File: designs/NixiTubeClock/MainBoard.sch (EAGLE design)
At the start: 17 parts, among them IC1 LD117ADT-TR, J1 S2B-PH-SM4, J2 S2B-PH-SM4, J3 S2B-PH-SM4, J4 S2B-PH-SM4, J7 S2B-PH-SM4, J8 S2B-PH-SM4

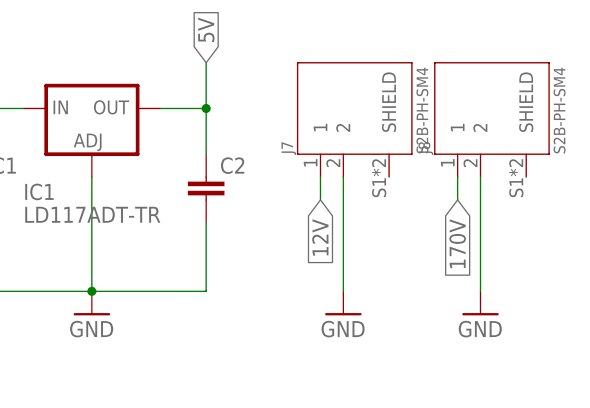
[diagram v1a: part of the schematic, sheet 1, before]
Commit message: added parts for nixi clock final check during the week
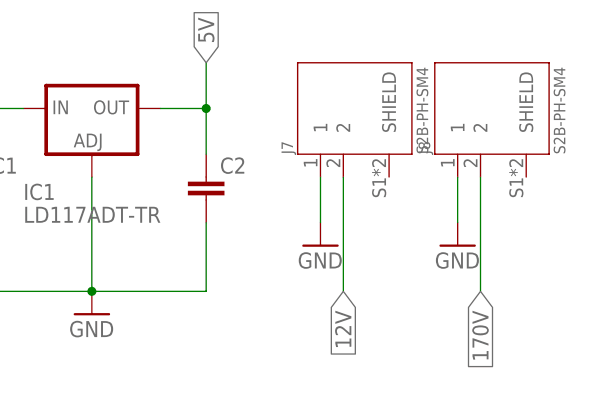
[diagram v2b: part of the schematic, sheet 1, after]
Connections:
- net 12V: now also J7.2; no longer J7.1
- net 170V: now also J8.2; no longer J8.1
- net GND: now also J7.1, J8.1; no longer J7.2, J8.2
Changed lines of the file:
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@@
 <?xml version="1.0" encoding="utf-8"?>
 <!DOCTYPE eagle SYSTEM "eagle.dtd">
-<eagle version="9.5.2">
+<eagle version="9.5.1">
 <drawing>
 <settings>
@@
 <part name="GND5" library="supply1" library_urn="urn:adsk.eagle:library:371" deviceset="GND" device=""/>
 <part name="GND6" library="supply1" library_urn="urn:adsk.eagle:library:371" deviceset="GND" device=""/>
-<part name="GND7" library="supply1" library_urn="urn:adsk.eagle:library:371" deviceset="GND" device=""/>
-<part name="GND8" library="supply1" library_urn="urn:adsk.eagle:library:371" deviceset="GND" device=""/>
 <part name="IC1" library="nixie_tube" deviceset="LD117A?*" device="DT" package3d_urn="urn:adsk.eagle:package:30369/1" technology="-TR"/>
 <part name="C1" library="CommonParts" deviceset="C-EU_1206" device="C1206" package3d_urn="urn:adsk.eagle:package:23618/2"/>
 <part name="C2" library="CommonParts" deviceset="C-EU_1206" device="C1206" package3d_urn="urn:adsk.eagle:package:23618/2"/>
 <part name="GND9" library="supply1" library_urn="urn:adsk.eagle:library:371" deviceset="GND" device=""/>
+<part name="GND8" library="supply1" library_urn="urn:adsk.eagle:library:371" deviceset="GND" device=""/>
+<part name="GND7" library="supply1" library_urn="urn:adsk.eagle:library:371" deviceset="GND" device=""/>
 </parts>
 <sheets>
@@
 <attribute name="VALUE" x="210.82" y="91.44" size="1.778" layer="96"/>
 </instance>
-<instance part="GND7" gate="1" x="193.04" y="48.26" smashed="yes">
-<attribute name="VALUE" x="190.5" y="45.72" size="1.778" layer="96"/>
-</instance>
-<instance part="GND8" gate="1" x="208.28" y="48.26" smashed="yes">
-<attribute name="VALUE" x="205.74" y="45.72" size="1.778" layer="96"/>
-</instance>
 <instance part="IC1" gate="G$1" x="165.1" y="71.12" smashed="yes">
 <attribute name="NAME" x="157.48" y="60.96" size="1.778" layer="95"/>
@@
 <instance part="GND9" gate="1" x="165.1" y="48.26" smashed="yes">
 <attribute name="VALUE" x="162.56" y="45.72" size="1.778" layer="96"/>
+</instance>
+<instance part="GND8" gate="1" x="190.5" y="55.88" smashed="yes">
+<attribute name="VALUE" x="187.96" y="53.34" size="1.778" layer="96"/>
+</instance>
+<instance part="GND7" gate="1" x="205.74" y="55.88" smashed="yes">
+<attribute name="VALUE" x="203.2" y="53.34" size="1.778" layer="96"/>
 </instance>
 </instances>
@@
 <wire x1="213.36" y1="109.22" x2="213.36" y2="96.52" width="0.1524" layer="91"/>
 <pinref part="GND6" gate="1" pin="GND"/>
-</segment>
-<segment>
-<pinref part="J7" gate="G$1" pin="2"/>
-<pinref part="GND7" gate="1" pin="GND"/>
-<wire x1="193.04" y1="50.8" x2="193.04" y2="63.5" width="0.1524" layer="91"/>
-</segment>
-<segment>
-<pinref part="J8" gate="G$1" pin="2"/>
-<pinref part="GND8" gate="1" pin="GND"/>
-<wire x1="208.28" y1="63.5" x2="208.28" y2="50.8" width="0.1524" layer="91"/>
 </segment>
 <segment>
@@
 <pinref part="SV4" gate="1" pin="5"/>
 </segment>
+<segment>
+<pinref part="GND8" gate="1" pin="GND"/>
+<pinref part="J7" gate="G$1" pin="1"/>
+<wire x1="190.5" y1="58.42" x2="190.5" y2="63.5" width="0.1524" layer="91"/>
+</segment>
+<segment>
+<pinref part="J8" gate="G$1" pin="1"/>
+<pinref part="GND7" gate="1" pin="GND"/>
+<wire x1="205.74" y1="58.42" x2="205.74" y2="63.5" width="0.1524" layer="91"/>
+</segment>
 </net>
 <net name="3.3V" class="0">
@@
 <net name="12V" class="0">
 <segment>
-<pinref part="J7" gate="G$1" pin="1"/>
-<wire x1="190.5" y1="63.5" x2="190.5" y2="60.96" width="0.1524" layer="91"/>
-<label x="190.5" y="60.96" size="1.778" layer="95" rot="R270" xref="yes"/>
-</segment>
-<segment>
 <pinref part="C1" gate="G$1" pin="1"/>
 <wire x1="152.4" y1="66.04" x2="152.4" y2="71.12" width="0.1524" layer="91"/>
@@
 <label x="152.4" y="76.2" size="1.778" layer="95" rot="R90" xref="yes"/>
 </segment>
+<segment>
+<pinref part="J7" gate="G$1" pin="2"/>
+<wire x1="193.04" y1="50.8" x2="193.04" y2="63.5" width="0.1524" layer="91"/>
+<label x="193.04" y="50.8" size="1.778" layer="95" rot="R270" xref="yes"/>
+</segment>
 </net>
 <net name="170V" class="0">
-<segment>
-<pinref part="J8" gate="G$1" pin="1"/>
-<wire x1="205.74" y1="63.5" x2="205.74" y2="60.96" width="0.1524" layer="91"/>
-<label x="205.74" y="60.96" size="1.778" layer="95" rot="R270" xref="yes"/>
-</segment>
 <segment>
 <wire x1="78.74" y1="119.38" x2="81.28" y2="119.38" width="0.1524" layer="91"/>
@@
 <pinref part="SV4" gate="1" pin="6"/>
 </segment>
-</net>
+<segment>
+<pinref part="J8" gate="G$1" pin="2"/>
+<wire x1="208.28" y1="63.5" x2="208.28" y2="50.8" width="0.1524" layer="91"/>
+<label x="208.28" y="50.8" size="1.778" layer="95" rot="R270" xref="yes"/>
+</segment>
+</net>

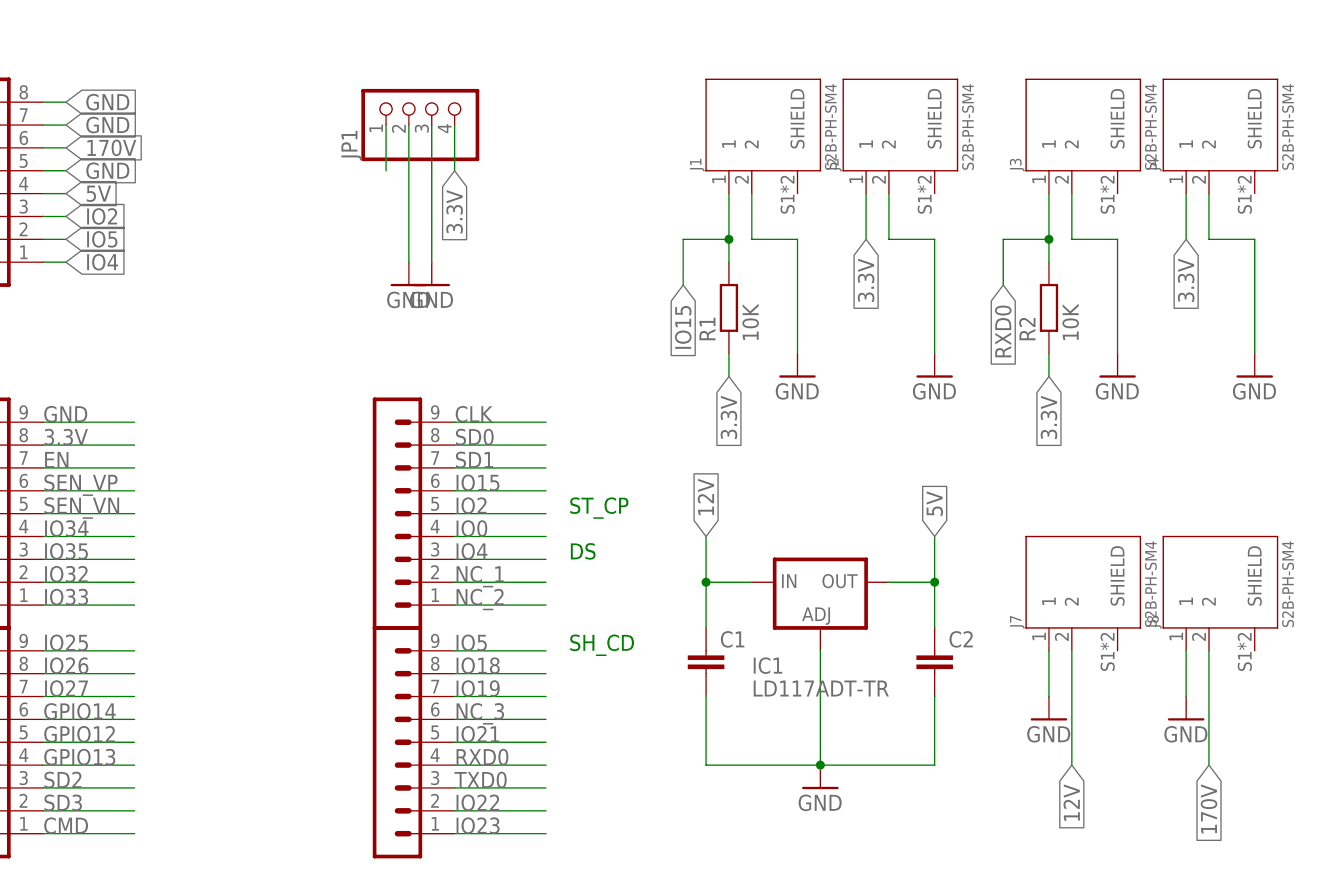
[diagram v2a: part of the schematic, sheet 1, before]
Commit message: added parts for nixi clock final check during the week
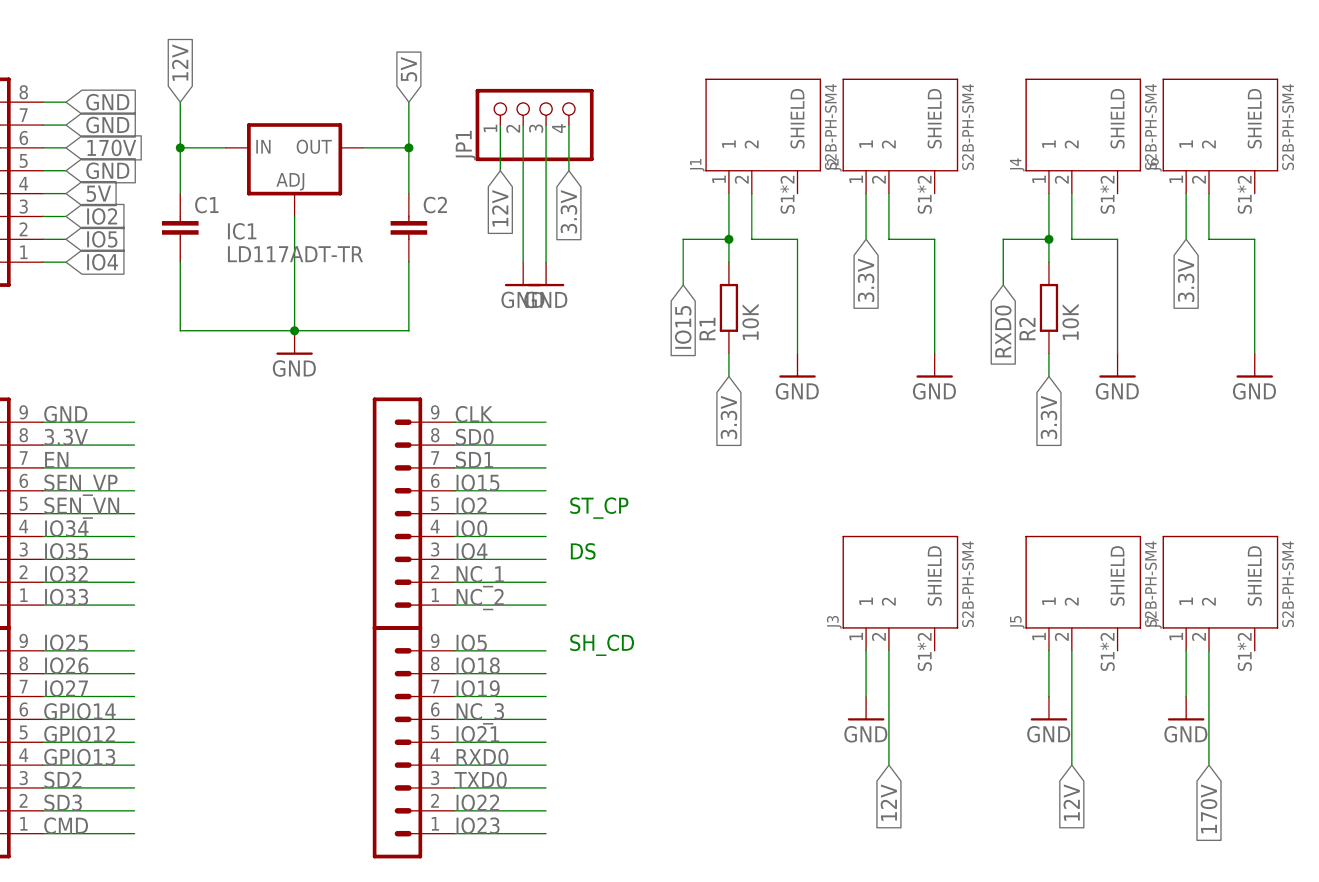
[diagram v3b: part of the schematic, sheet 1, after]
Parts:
- removed J8: S2B-PH-SM4, CommonParts:S2B-PH-SM4
- removed SV6: (no value), CommonParts:PINHEADER-1X9
- added J5, J6: S2B-PH-SM4, CommonParts:S2B-PH-SM4
- added SV1: (no value), CommonParts:PINHEADER-1X8
- SV4: device CommonParts:PINHEADER-1X8 -> CommonParts:PINHEADER-1X9
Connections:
- removed net NC: JP1.1
- net 12V: now also J3.2, J5.2, JP1.1; no longer J7.2
- net 170V: now also J7.2, SV1.6; no longer J8.2, SV4.6
- net 3.3V: now also J6.1, SV2.8; no longer J4.1, SV5.8
- net 5V: now also SV1.4; no longer SV4.4
- net CLK: now also SV4.9; no longer SV2.9
- net CMD: now also SV3.1; no longer SV6.1
- net EN: now also SV2.7; no longer SV5.7
- net GND: now also J3.1, J5.1, J6.2, SV1.5, SV1.7, SV1.8, SV2.9; no longer J3.2, J8.1, SV4.5, SV4.7, SV4.8, SV5.9
- net GPIO12: now also SV3.5; no longer SV6.5
- net GPIO13: now also SV3.4; no longer SV6.4
- net GPIO14: now also SV3.6; no longer SV6.6
- net IO0: now also SV4.4; no longer SV2.4
- net IO15: now also SV4.6; no longer SV2.6
- net IO18: now also SV5.8; no longer SV3.8
- net IO19: now also SV5.7; no longer SV3.7
- net IO2: now also SV1.3, SV4.5; no longer SV2.5, SV4.3
- net IO21: now also SV5.5; no longer SV3.5
- net IO22: now also SV5.2; no longer SV3.2
- net IO23: now also SV5.1; no longer SV3.1
- net IO25: now also SV3.9; no longer SV6.9
- net IO26: now also SV3.8; no longer SV6.8
- net IO27: now also SV3.7; no longer SV6.7
- net IO32: now also SV2.2; no longer SV5.2
- net IO33: now also SV2.1; no longer SV5.1
- net IO34: now also SV2.4; no longer SV5.4
- net IO35: now also SV2.3; no longer SV5.3
- net IO4: now also SV1.1, SV4.3; no longer SV2.3, SV4.1
- net IO5: now also SV1.2, SV5.9; no longer SV3.9, SV4.2
- net NC_1: now also SV4.2; no longer SV2.2
- net NC_2: now also SV4.1; no longer SV2.1
- net NC_3: now also SV5.6; no longer SV3.6
- net RXD0: now also J4.1, SV5.4; no longer J3.1, SV3.4
- net SD0: now also SV4.8; no longer SV2.8
- net SD1: now also SV4.7; no longer SV2.7
- net SD2: now also SV3.3; no longer SV6.3
- net SD3: now also SV3.2; no longer SV6.2
- net SEN_VN: now also SV2.5; no longer SV5.5
- net SEN_VP: now also SV2.6; no longer SV5.6
- net TXD0: now also SV5.3; no longer SV3.3
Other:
- moved on the sheet: C1, C2, IC1, J3, J4, J7, JP1

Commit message: started work on mainboard
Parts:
- removed J3, J7: S2B-PH-SM4, CommonParts:S2B-PH-SM4
- added SV6: (no value), CommonParts:PINHEADER-1X8
- J5: value S2B-PH-SM4 -> PJ-002AH-SMT-TR; device CommonParts:S2B-PH-SM4 -> CommonParts:PJ-002AH-SMT-TR
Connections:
- net 12V: no longer J3.2, J5.2
- net 170V: no longer J7.2
- net GND: no longer J3.1, J5.1, J7.1
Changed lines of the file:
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@@
 <layer number="121" name="_tsilk" color="7" fill="1" visible="yes" active="yes"/>
 <layer number="122" name="_bsilk" color="7" fill="1" visible="yes" active="yes"/>
+<layer number="125" name="_tNames" color="7" fill="1" visible="no" active="yes"/>
+<layer number="127" name="Display" color="11" fill="1" visible="yes" active="yes"/>
 <layer number="131" name="prix" color="7" fill="1" visible="yes" active="yes"/>
 <layer number="132" name="test" color="7" fill="1" visible="yes" active="yes"/>
+<layer number="144" name="Drill_legend" color="7" fill="1" visible="no" active="yes"/>
 <layer number="151" name="HeatSink" color="7" fill="1" visible="yes" active="yes"/>
 <layer number="200" name="200bmp" color="7" fill="1" visible="yes" active="yes"/>
@@
 <layer number="207" name="207bmp" color="7" fill="1" visible="yes" active="yes"/>
 <layer number="208" name="208bmp" color="7" fill="1" visible="yes" active="yes"/>
+<layer number="209" name="209bmp" color="7" fill="1" visible="no" active="yes"/>
+<layer number="210" name="210bmp" color="7" fill="1" visible="no" active="yes"/>
+<layer number="211" name="211bmp" color="7" fill="1" visible="no" active="yes"/>
+<layer number="212" name="212bmp" color="7" fill="1" visible="no" active="yes"/>
+<layer number="213" name="213bmp" color="7" fill="1" visible="no" active="yes"/>
+<layer number="214" name="214bmp" color="7" fill="1" visible="no" active="yes"/>
+<layer number="215" name="215bmp" color="7" fill="1" visible="no" active="yes"/>
+<layer number="216" name="216bmp" color="7" fill="1" visible="no" active="yes"/>
+<layer number="217" name="217bmp" color="18" fill="1" visible="no" active="no"/>
+<layer number="218" name="218bmp" color="19" fill="1" visible="no" active="no"/>
+<layer number="219" name="219bmp" color="20" fill="1" visible="no" active="no"/>
+<layer number="220" name="220bmp" color="21" fill="1" visible="no" active="no"/>
+<layer number="221" name="221bmp" color="22" fill="1" visible="no" active="no"/>
+<layer number="222" name="222bmp" color="23" fill="1" visible="no" active="no"/>
+<layer number="223" name="223bmp" color="24" fill="1" visible="no" active="no"/>
+<layer number="224" name="224bmp" color="25" fill="1" visible="no" active="no"/>
 <layer number="250" name="Descript" color="7" fill="1" visible="yes" active="yes"/>
 <layer number="251" name="SMDround" color="7" fill="1" visible="yes" active="yes"/>
@@
 <part name="J4" library="CommonParts" deviceset="S2B-PH-SM4" device=""/>
 <part name="J6" library="CommonParts" deviceset="S2B-PH-SM4" device=""/>
-<part name="J5" library="CommonParts" deviceset="S2B-PH-SM4" device=""/>
-<part name="J7" library="CommonParts" deviceset="S2B-PH-SM4" device=""/>
 <part name="R1" library="CommonParts" deviceset="R-EU_1206" device="R1206" package3d_urn="urn:adsk.eagle:package:23540/2" value="10K"/>
 <part name="R2" library="CommonParts" deviceset="R-EU_1206" device="R1206" package3d_urn="urn:adsk.eagle:package:23540/2" value="10K"/>
@@
 <part name="C2" library="CommonParts" deviceset="C-EU_1206" device="C1206" package3d_urn="urn:adsk.eagle:package:23618/2"/>
 <part name="GND1" library="supply1" library_urn="urn:adsk.eagle:library:371" deviceset="GND" device=""/>
-<part name="GND7" library="supply1" library_urn="urn:adsk.eagle:library:371" deviceset="GND" device=""/>
-<part name="GND9" library="supply1" library_urn="urn:adsk.eagle:library:371" deviceset="GND" device=""/>
-<part name="J3" library="CommonParts" deviceset="S2B-PH-SM4" device=""/>
-<part name="GND5" library="supply1" library_urn="urn:adsk.eagle:library:371" deviceset="GND" device=""/>
+<part name="SV6" library="CommonParts" deviceset="PINHEADER-1X8" device="" package3d_urn="urn:adsk.eagle:package:8343/1"/>
+<part name="J5" library="CommonParts" deviceset="PJ-002AH-SMT-TR" device=""/>
 </parts>
 <sheets>
@@
 <attribute name="VALUE" x="217.70268125" y="116.83188125" size="1.275409375" layer="96" rot="R90"/>
 </instance>
-<instance part="J5" gate="G$1" x="193.04" y="71.12" smashed="yes" rot="R90">
-<attribute name="NAME" x="187.44428125" y="66.0371" size="1.272509375" layer="95" rot="R90"/>
-<attribute name="VALUE" x="202.46268125" y="66.03188125" size="1.275409375" layer="96" rot="R90"/>
-</instance>
-<instance part="J7" gate="G$1" x="208.28" y="71.12" smashed="yes" rot="R90">
-<attribute name="NAME" x="202.68428125" y="66.0371" size="1.272509375" layer="95" rot="R90"/>
-<attribute name="VALUE" x="217.70268125" y="66.03188125" size="1.275409375" layer="96" rot="R90"/>
-</instance>
 <instance part="R1" gate="G$1" x="154.94" y="101.6" smashed="yes" rot="R90">
 <attribute name="NAME" x="153.4414" y="97.79" size="1.778" layer="95" rot="R90"/>
@@
 <attribute name="VALUE" x="104.14" y="93.98" size="1.778" layer="96"/>
 </instance>
-<instance part="GND7" gate="1" x="190.5" y="55.88" smashed="yes">
-<attribute name="VALUE" x="187.96" y="53.34" size="1.778" layer="96"/>
-</instance>
-<instance part="GND9" gate="1" x="205.74" y="55.88" smashed="yes">
-<attribute name="VALUE" x="203.2" y="53.34" size="1.778" layer="96"/>
-</instance>
-<instance part="J3" gate="G$1" x="172.72" y="71.12" smashed="yes" rot="R90">
-<attribute name="NAME" x="167.12428125" y="66.0371" size="1.272509375" layer="95" rot="R90"/>
-<attribute name="VALUE" x="182.14268125" y="66.03188125" size="1.275409375" layer="96" rot="R90"/>
-</instance>
-<instance part="GND5" gate="1" x="170.18" y="55.88" smashed="yes">
-<attribute name="VALUE" x="167.64" y="53.34" size="1.778" layer="96"/>
+<instance part="SV6" gate="1" x="152.4" y="50.8" smashed="yes"/>
+<instance part="J5" gate="G$1" x="205.74" y="55.88" smashed="yes" rot="R180">
+<attribute name="NAME" x="186.69" y="48.26" size="1.778" layer="95" rot="R180" align="center-left"/>
+<attribute name="VALUE" x="186.69" y="50.8" size="1.778" layer="96" rot="R180" align="center-left"/>
 </instance>
 </instances>
@@
 <pinref part="SV1" gate="1" pin="5"/>
 </segment>
-<segment>
-<pinref part="GND7" gate="1" pin="GND"/>
-<pinref part="J5" gate="G$1" pin="1"/>
-<wire x1="190.5" y1="58.42" x2="190.5" y2="63.5" width="0.1524" layer="91"/>
-</segment>
-<segment>
-<pinref part="J7" gate="G$1" pin="1"/>
-<pinref part="GND9" gate="1" pin="GND"/>
-<wire x1="205.74" y1="58.42" x2="205.74" y2="63.5" width="0.1524" layer="91"/>
-</segment>
-<segment>
-<pinref part="GND5" gate="1" pin="GND"/>
-<pinref part="J3" gate="G$1" pin="1"/>
-<wire x1="170.18" y1="58.42" x2="170.18" y2="63.5" width="0.1524" layer="91"/>
-</segment>
 </net>
 <net name="3.3V" class="0">
@@
 </segment>
 <segment>
-<pinref part="J5" gate="G$1" pin="2"/>
-<wire x1="193.04" y1="50.8" x2="193.04" y2="63.5" width="0.1524" layer="91"/>
-<label x="193.04" y="50.8" size="1.778" layer="95" rot="R270" xref="yes"/>
-</segment>
-<segment>
 <pinref part="JP1" gate="A" pin="1"/>
 <wire x1="129.54" y1="121.92" x2="129.54" y2="116.84" width="0.1524" layer="91"/>
 <label x="129.54" y="116.84" size="1.778" layer="95" rot="R270" xref="yes"/>
 </segment>
-<segment>
-<pinref part="J3" gate="G$1" pin="2"/>
-<wire x1="172.72" y1="50.8" x2="172.72" y2="63.5" width="0.1524" layer="91"/>
-<label x="172.72" y="50.8" size="1.778" layer="95" rot="R270" xref="yes"/>
-</segment>
 </net>
 <net name="170V" class="0">
@@
 <pinref part="SV1" gate="1" pin="6"/>
 </segment>
-<segment>
-<pinref part="J7" gate="G$1" pin="2"/>
-<wire x1="208.28" y1="63.5" x2="208.28" y2="50.8" width="0.1524" layer="91"/>
-<label x="208.28" y="50.8" size="1.778" layer="95" rot="R270" xref="yes"/>
-</segment>
-</net>
+</net>
